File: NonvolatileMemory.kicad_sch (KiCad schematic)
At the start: 8 parts, among them J6 Micro_SD_Card_Det_Hirose_DM3AT, U4 MX25R3235FZNxx1, U9 TPS22917DBV

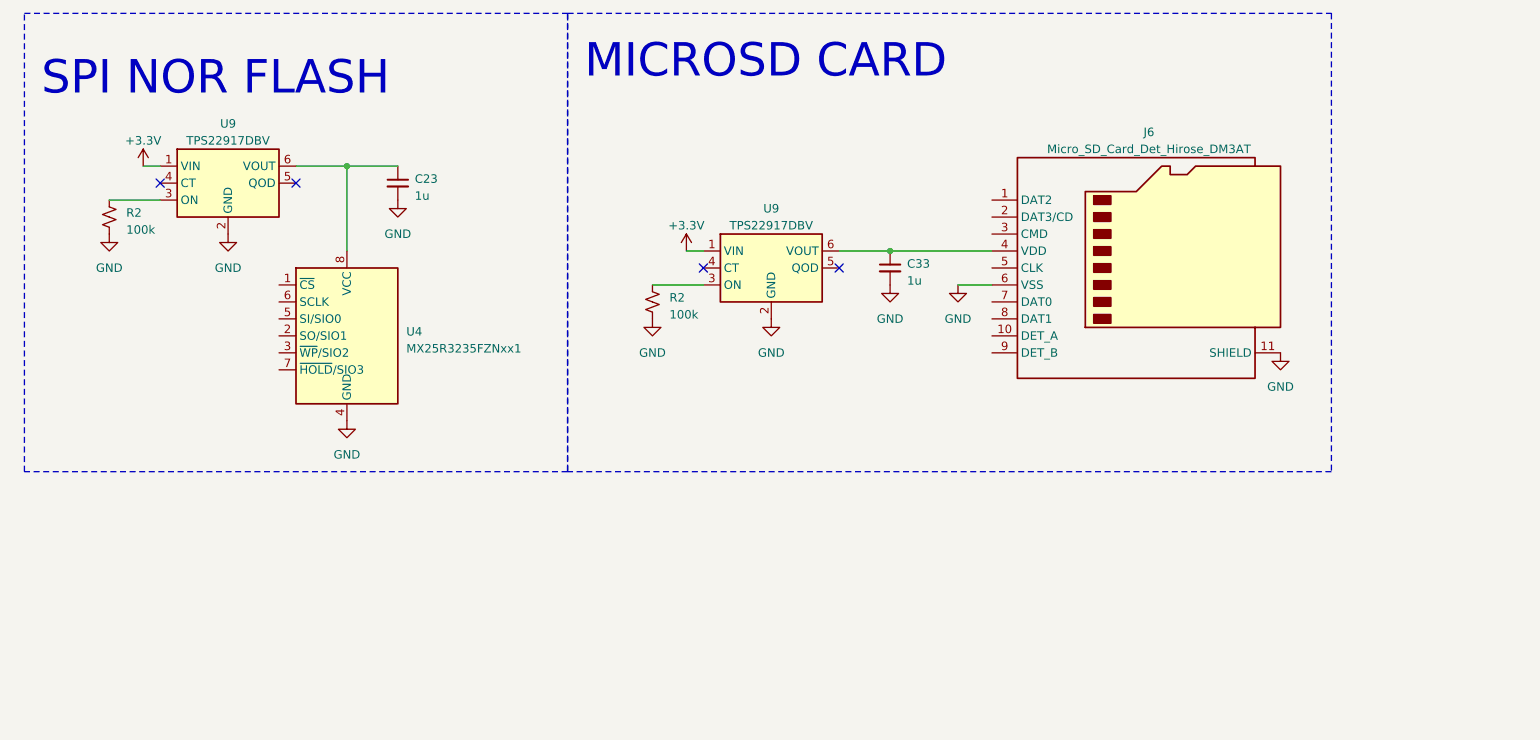
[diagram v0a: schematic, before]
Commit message: Added passvies and bus connections to nRF7002
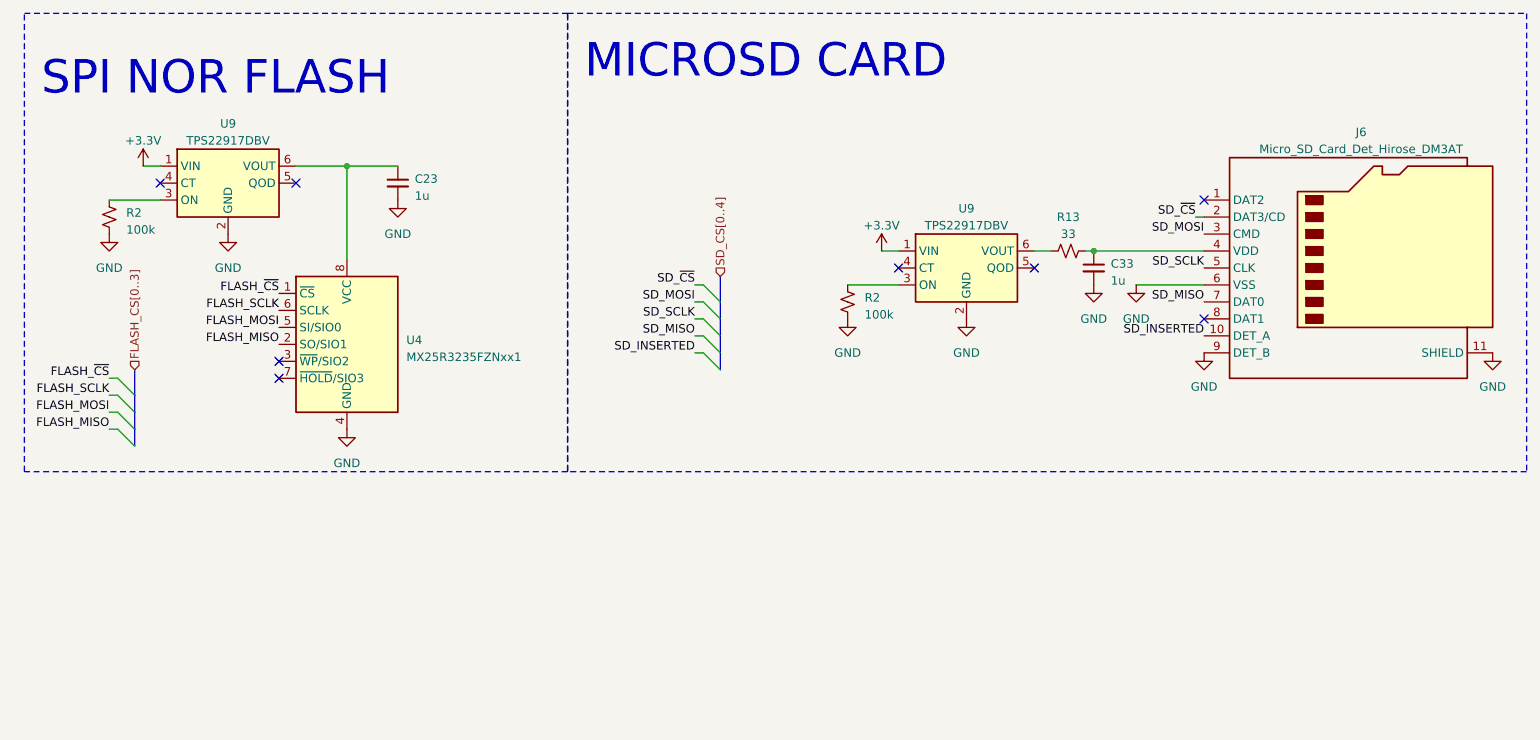
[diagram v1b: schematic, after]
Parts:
- added R13: 33, symbol Device:R_Small_US
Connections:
- net GND: now also J6.9 (DET_B)
- net FLASH_~{CS}: now reaches U4.1 (~{CS})
- net FLASH_MISO: now reaches U4.2 (SO/SIO1)
- net FLASH_MOSI: now reaches U4.5 (SI/SIO0)
- net FLASH_SCLK: now reaches U4.6 (SCLK)
- net SD_INSERTED: now reaches J6.10 (DET_A)
- net SD_~{CS}: now reaches J6.2 (DAT3/CD)
- net SD_MOSI: now reaches J6.3 (CMD)
- net at C33.1, J6.4 (VDD): now also R13.2; no longer U9.6 (VOUT)
- net SD_SCLK: now reaches J6.5 (CLK)
- net SD_MISO: now reaches J6.7 (DAT0)
- new net: R13.1, U9.6 (VOUT)
- no-connect marks 4 -> 8
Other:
- moved on the sheet: C33, J6, R2, U4, U9

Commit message: Schematic complete.
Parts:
- removed C23: 1u, symbol Device:C_Small
- removed R2: 100k, symbol Device:R_Small_US
- removed U9: TPS22917DBV, Package_TO_SOT_SMD:SOT-23-6, symbol Power_Management:TPS22917DBV
- C33: footprint (none) -> Capacitor_SMD:C_0402_1005Metric
- R13, R2: footprint (none) -> Resistor_SMD:R_0603_1608Metric
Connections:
- net SD_MISO is gone; now on net FLASH_MISO: J6.7 (DAT0)
- net SD_MOSI is gone; now on net FLASH_MOSI: J6.3 (CMD)
- net SD_SCLK is gone; now on net FLASH_SCLK: J6.5 (CLK)
- net FLASH_VDD_IN: now reaches U4.8 (VCC)
- net SD_CARD_EN: now reaches R2.1, U9.3 (ON)
- net FLASH_~{CS} renamed FLASH_SD_CTRL0
- net SD_~{CS} renamed FLASH_SD_CTRL4
- no-connect marks 8 -> 6
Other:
- moved on the sheet: C33, J6, R13, R2, U4, U9
